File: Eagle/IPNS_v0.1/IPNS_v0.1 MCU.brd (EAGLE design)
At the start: 32.7 x 33 mm, 30 parts, among them J1 SWIM, J2 NFC, J3 BATT, J4 RIGHT CONN, J5 LEFT CONN, Q1 16MHz, Q2 32.768 kHz, U1 STM8L152C4_C6TX

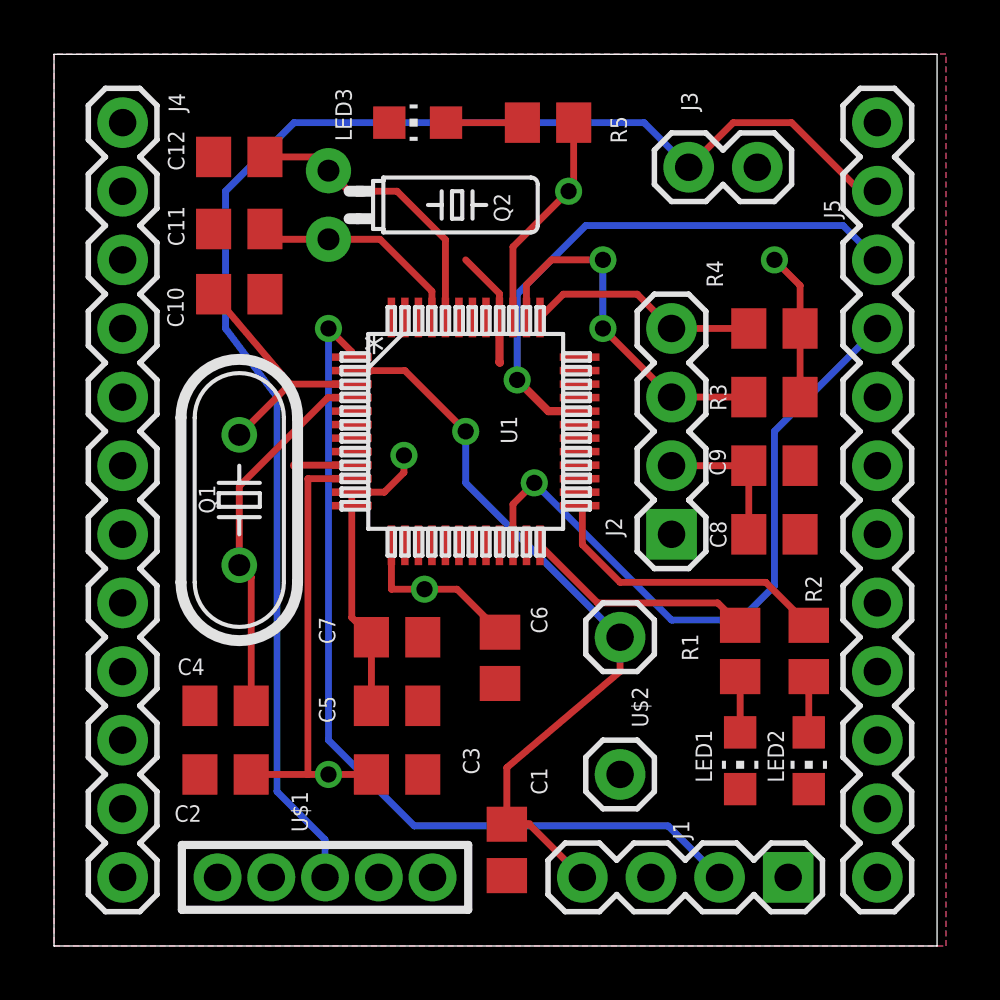
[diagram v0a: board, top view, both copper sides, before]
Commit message: Broke out more pins on the MCU module
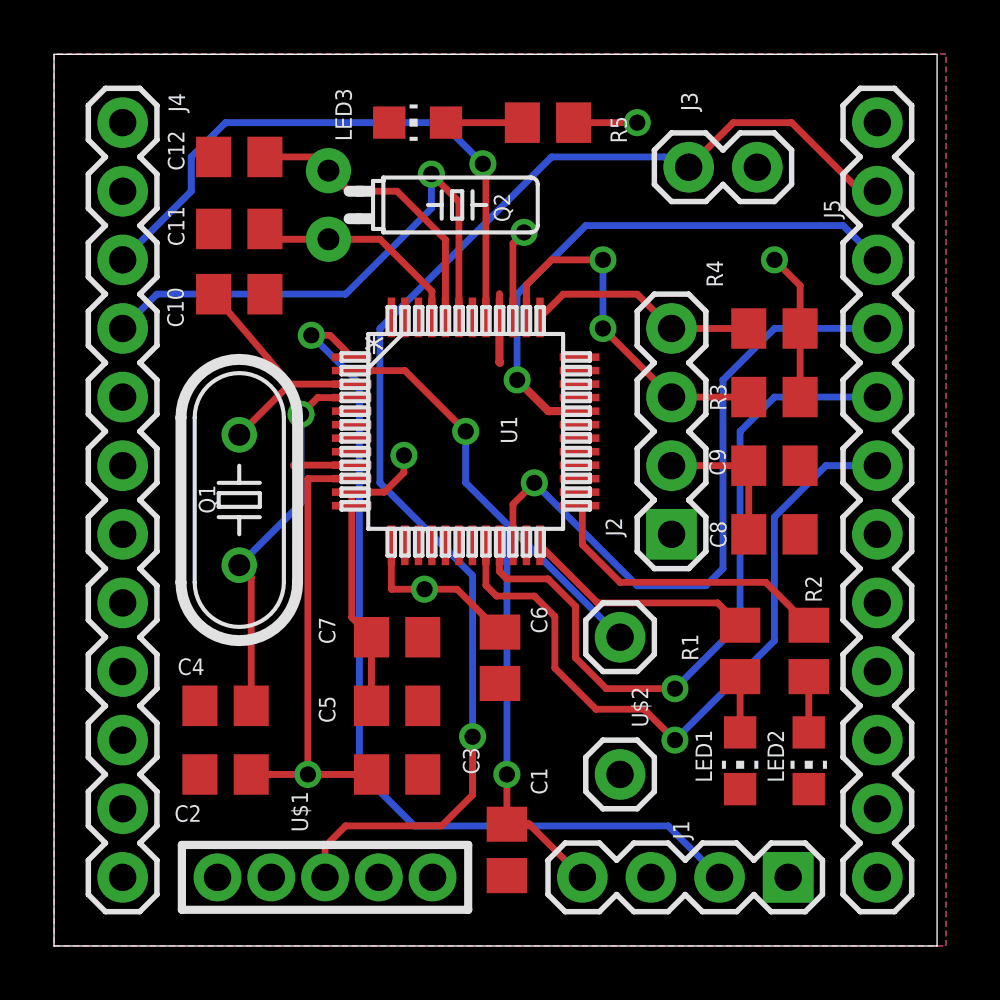
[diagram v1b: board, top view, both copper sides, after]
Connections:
- new net PC4: J4.4, U1.43
- new net PD0: J5.6, U1.20
- new net PD1: J5.5, U1.21
- new net VREFINT: J4.3, U1.41
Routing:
- net PD1: track 0.00 -> 26.5 mm, vias 0 -> 1
- net PD0: track 0.00 -> 26.4 mm, vias 0 -> 1
- net VREFINT: track 0.00 -> 22.9 mm, vias 0 -> 1
- net PC4: track 0.00 -> 20.3 mm, vias 0 -> 1
- net VBATT: track 54.4 -> 49.0 mm, vias 0 -> 1
- net +3V3: track 53.4 -> 51.0 mm, vias 5 -> 6
- net RESET: track 28.3 -> 30.5 mm, vias 1 -> 2
- net GND: track 6.49 -> 4.72 mm
- net N$5: track 13.8 -> 14.1 mm, vias 0 -> 1

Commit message: Two PCBs clearances adjusted
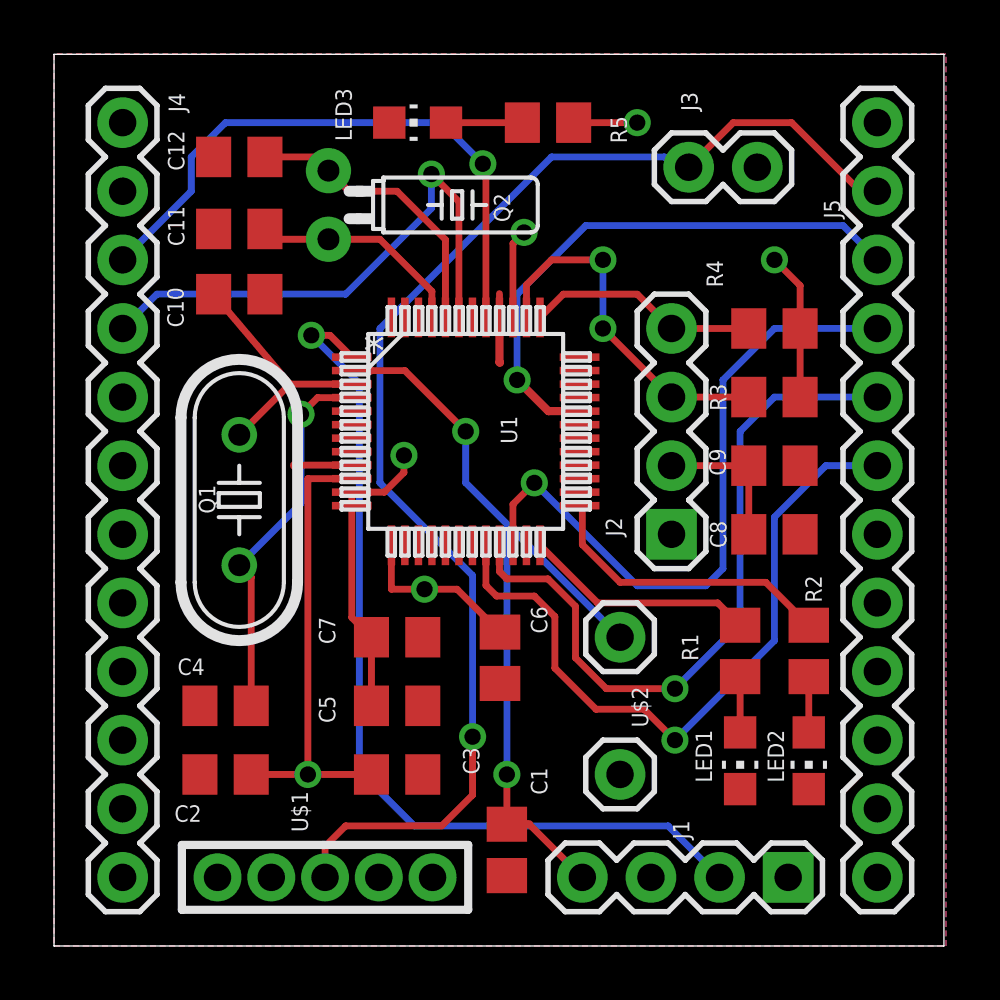
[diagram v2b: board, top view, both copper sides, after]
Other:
- board size 32.7 x 33 mm -> 32.9 x 33 mm
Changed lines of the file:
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@@
 <board>
 <plain>
-<wire x1="0" y1="0" x2="32.69" y2="0" width="0" layer="20"/>
-<wire x1="32.69" y1="0" x2="32.69" y2="33.01" width="0" layer="20"/>
-<wire x1="32.69" y1="33.01" x2="0" y2="33.01" width="0" layer="20"/>
+<wire x1="0" y1="0" x2="32.944" y2="0" width="0" layer="20"/>
+<wire x1="32.944" y1="0" x2="32.944" y2="33.01" width="0" layer="20"/>
+<wire x1="32.944" y1="33.01" x2="0" y2="33.01" width="0" layer="20"/>
 <wire x1="0" y1="33.01" x2="0" y2="0" width="0" layer="20"/>
 <text x="27.305" y="25.273" size="1.778" layer="22" rot="MR270">IPNS_v0.1 MCU</text>
@@
 <contactref element="U1" pad="12"/>
 <contactref element="R5" pad="2"/>
-<polygon width="0.4064" layer="16">
+<polygon width="0.254" layer="16" isolate="0.2032">
 <vertex x="0" y="33.02"/>
 <vertex x="0" y="0"/>
@@
 <contactref element="J2" pad="1"/>
 <contactref element="C9" pad="1"/>
-<polygon width="0.4064" layer="1">
+<polygon width="0.254" layer="1" isolate="0.254">
 <vertex x="0" y="33.02"/>
 <vertex x="0" y="0"/>
